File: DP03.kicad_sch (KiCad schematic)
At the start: 21 parts

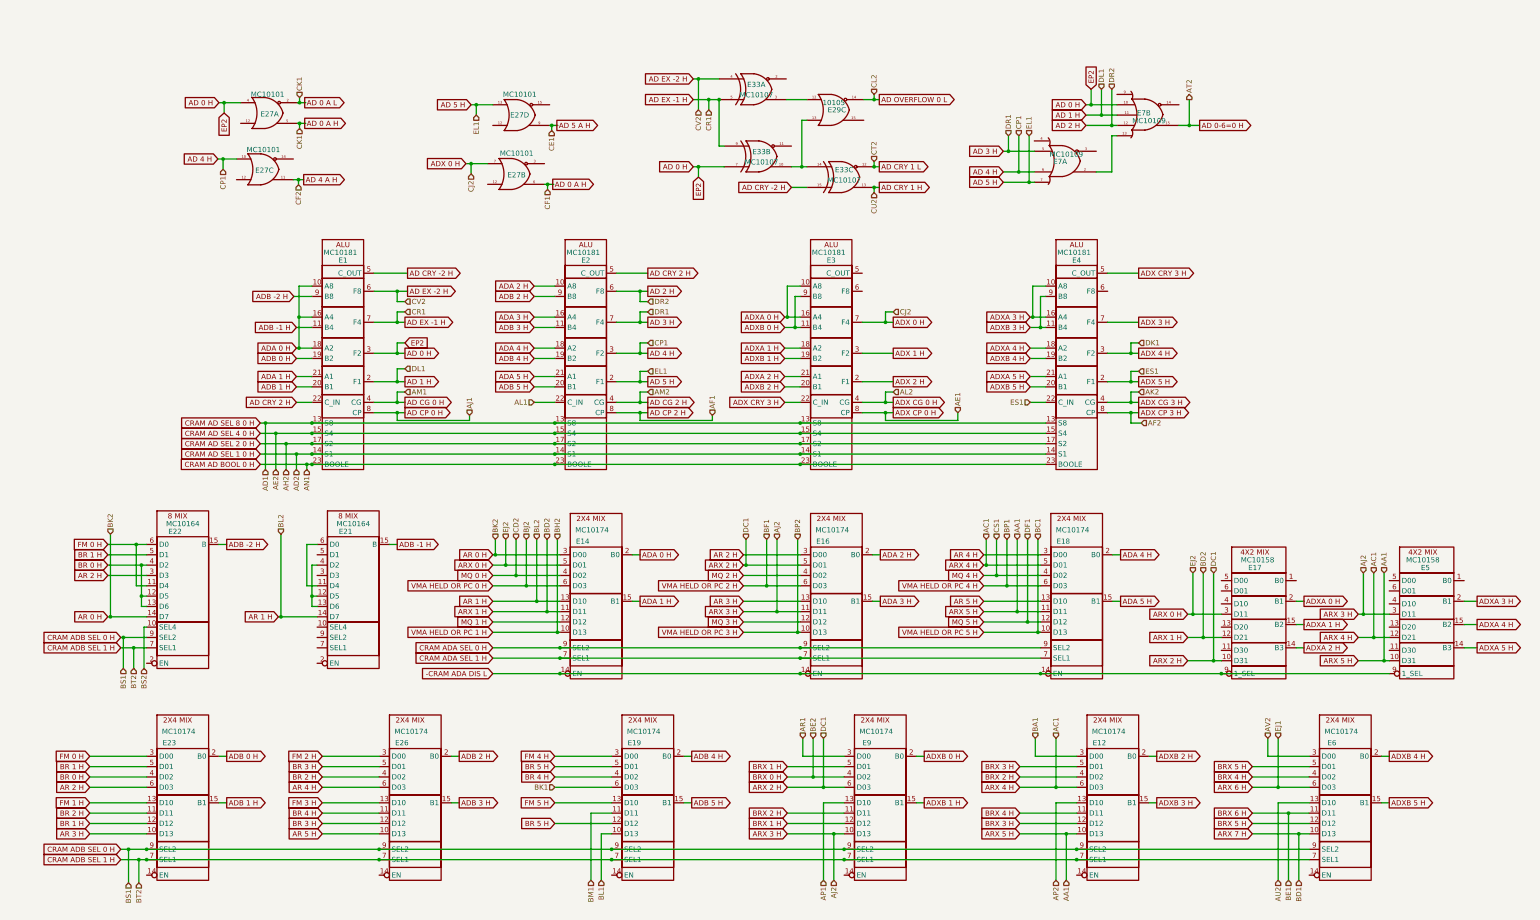
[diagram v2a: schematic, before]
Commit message: Convert all backplane refs to global labels and stick them on J1 pins. Convert all signal labels to global labels too so they are "global" inside M8512 board.
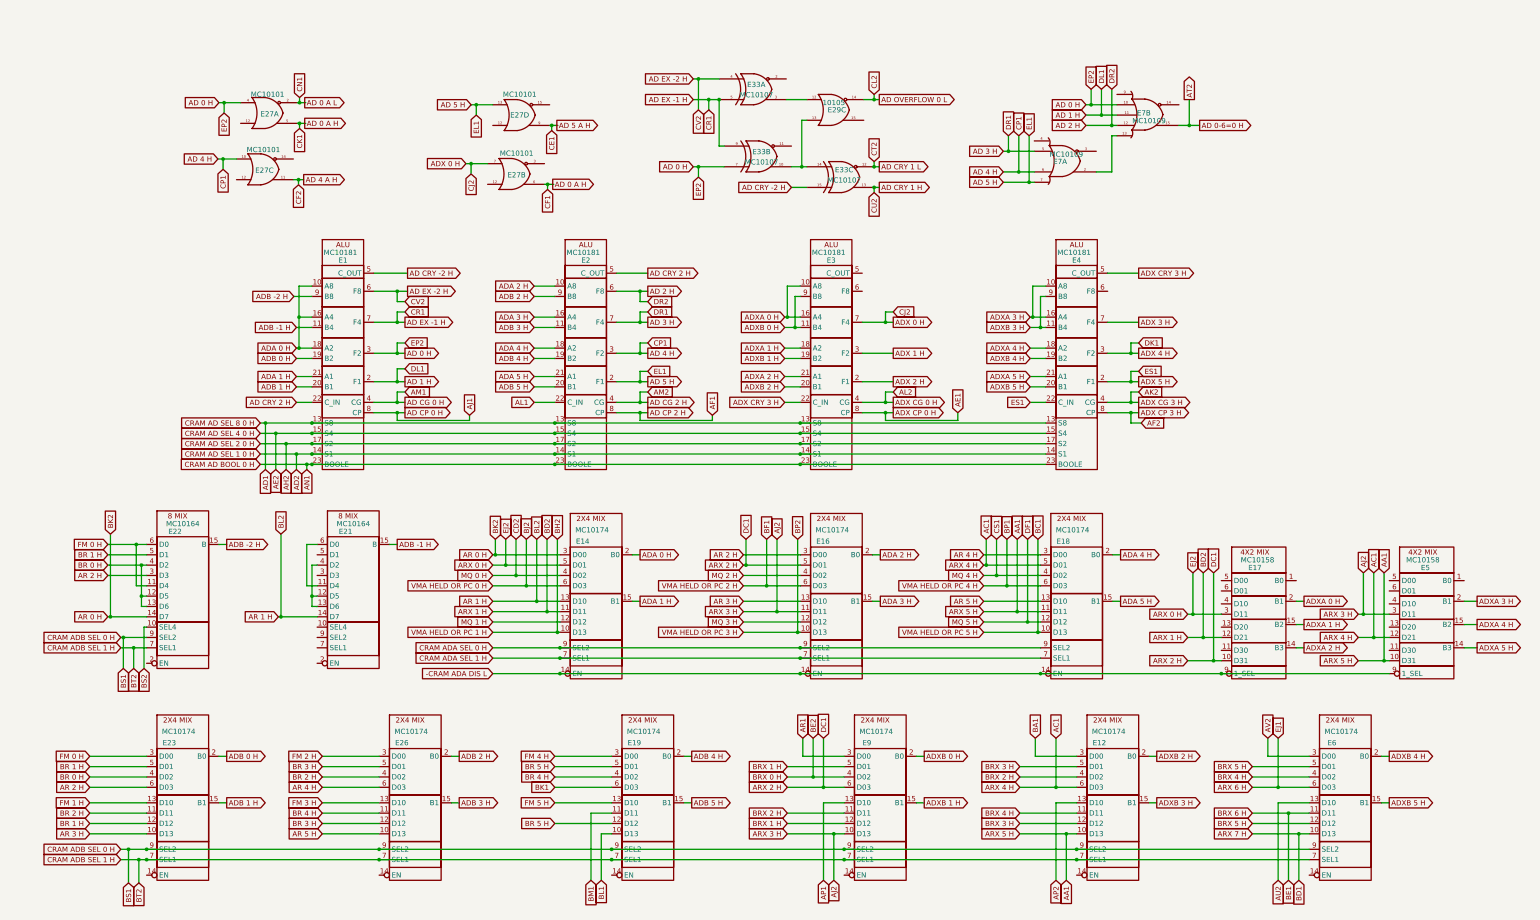
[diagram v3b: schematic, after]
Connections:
- net AD 0 A H: no longer E27.2 (~Aout)
- net ARX 3 H renamed AJ2
- net ARX 4 H renamed AC1
- net ARX 5 H renamed AA1
- net BRX 0 H renamed BE2
- net BRX 6 H renamed BE1
- net CRAM AD BOOL 0 H renamed AN1
- net CRAM AD SEL 1 0 H renamed AD2
- net CRAM AD SEL 2 0 H renamed AH2
- net CRAM AD SEL 4 0 H renamed AE2
- net CRAM AD SEL 8 0 H renamed AD1
- net CRAM ADB SEL 0 H renamed BS1
- net CRAM ADB SEL 1 H renamed BT2
- net MQ 0 H renamed CD2
- net MQ 4 H renamed CS1
- net MQ 5 H renamed DF1
- net VMA HELD OR PC 0 H renamed BJ2
- net VMA HELD OR PC 1 H renamed BH2
- net VMA HELD OR PC 2 H renamed BF1
- net VMA HELD OR PC 3 H renamed BP2
- net VMA HELD OR PC 4 H renamed BP1
- net VMA HELD OR PC 5 H renamed BC1
- new net AD 0 A L: E27.2 (~Aout)

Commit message: checkpoint
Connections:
- net AA1 renamed ARX 5 H <AA1>
- net AC1 renamed ARX 4 H <AC1>
- net AD 0 A H renamed AD 0 A H <CF1>
- net AD 0 A H <CF1>: no longer E27.5 (Aout)
- net AD 0 A L renamed AD 0 A L <CN1>
- net AD 0 H renamed AD 0 H <EP2>
- net AD 0-6=0 H renamed AD 0-6=0 H <AT2>
- net AD 1 H renamed AD 1 H <DL1>
- net AD 2 H renamed AD 2 H <DR2>
- net AD 3 H renamed AD 3 H <DR1>
- net AD 4 A H renamed AD 4 A H <CF2>
- net AD 4 H renamed AD 4 H <CP1>
- net AD 5 A H renamed AD 5 A H <CE1>
- net AD 5 H renamed AD 5 H <EL1>
- net AD CG 0 H renamed AD CG 0 H <AM1>
- net AD CG 2 H renamed AD CG 2 H <AM2>
- net AD CP 0 H renamed AD CP 0 H <AJ1>
- net AD CP 2 H renamed AD CP 2 H <AF1>
- net AD CRY 1 H renamed AD CRY 1 H <CU2>
- net AD CRY 1 L renamed AD CRY 1 L <CT2>
- net AD EX -1 H renamed AD EX -1 H <CR1>
- net AD EX -2 H renamed AD EX -2 H <CV2>
- net AD OVERFLOW 0 L renamed AD OVERFLOW 0 L <CL2>
- net AD1 renamed CRAM AD SEL 8 0 H <AD1>
- net AD2 renamed CRAM AD SEL 1 0 H <AD2>
- net ADX 0 H renamed ADX 0 H <CJ2>
- net ADX 4 H renamed ADX 4 H <DK1>
- net ADX 5 H renamed <ES1>
- net <ES1>: no longer E4.2 (F1)
- net ADX CG 0 H renamed ADX CG 0 H <AL2>
- net ADX CG 3 H renamed ADX CG 3 H <AK2>
- net ADX CP 0 H renamed ADX CP 0 H <AE1>
- net ADX CP 3 H renamed ADX CP 3 H <AF2>
- net AE2 renamed CRAM AD SEL 4 0 H <AE2>
- net AH2 renamed CRAM AD SEL 2 0 H <AH2>
- net AJ2 renamed ARX 3 H <AJ2>
- net AL1 renamed <AL1>
- net AN1 renamed CRAM AD BOOL 0 H <AN1>
- net AP1 renamed <AP1>
- net AP2 renamed <AP2>
- net AR 0 H renamed AR 0 H <BK2>
- net AR 1 H renamed AR 1 H <BL2>
- net AR1 renamed <AR1>
- net ARX 0 H renamed ARX 0 H <EJ2>
- net ARX 1 H renamed ARX 1 H <BD2>
- net ARX 2 H renamed ARX 2 H <DC1>
- net ARX 6 H renamed ARX 6 H <EJ1>
- net ARX 7 H renamed ARX 7 H <BD1>
- net AU2 renamed <AU2>
- net AV2 renamed <AV2>
- net BA1 renamed <BA1>
- net BC1 renamed VMA HELD OR PC 5 H <BC1>
- net BE1 renamed BRX 6 H <BE1>
- net BE2 renamed BRX 0 H <BE2>
- net BF1 renamed VMA HELD OR PC 2 H <BF1>
- net BH2 renamed VMA HELD OR PC 1 H <BH2>
- net BJ2 renamed VMA HELD OR PC 0 H <BJ2>
- net BK1 renamed <BK1>
- net BL1 renamed <BL1>
- net BM1 renamed <BM1>
- net BP1 renamed VMA HELD OR PC 4 H <BP1>
- net BP2 renamed VMA HELD OR PC 3 H <BP2>
- net BS1 renamed CRAM ADB SEL 0 H <BS1>
- net BS2 renamed <BS2>
- net BT2 renamed CRAM ADB SEL 1 H <BT2>
- net CD2 renamed MQ 0 H <CD2>
- net CS1 renamed MQ 4 H <CS1>
- net DF1 renamed MQ 5 H <DF1>
- new net AD 0 A H <CK1>: E27.5 (Aout)
- new net ADX 5 H <ES1>: E4.2 (F1)
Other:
- moved on the sheet: E7A, E7B

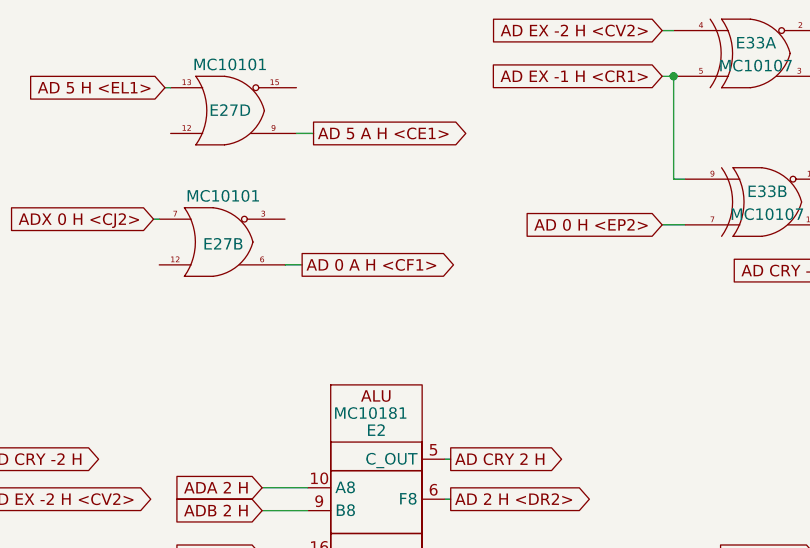
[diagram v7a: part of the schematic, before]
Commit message: Fix a bunch of typos and their backplane signal names
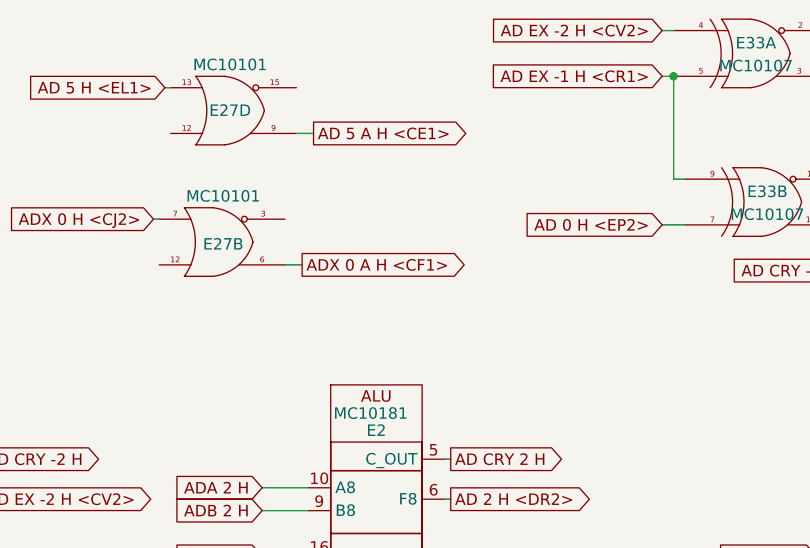
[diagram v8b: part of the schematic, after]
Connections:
- net AD 0 A H <CF1> renamed ADX 0 A H <CF1>
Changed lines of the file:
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@@
     )
   )
-  (global_label "AD 0 A H <CF1>" (shape output) (at 179.705 54.61 0) (fields_autoplaced)
+  (global_label "ADX 0 A H <CF1>" (shape output) (at 179.705 54.61 0) (fields_autoplaced)
     (effects (font (size 1.27 1.27)) (justify left))
-    (property "Intersheet References" "${INTERSHEET_REFS}" (id 0) (at 198.6886 54.5306 0)
+    (property "Intersheet References" "${INTERSHEET_REFS}" (id 0) (at 199.8981 54.5306 0)
       (effects (font (size 1.27 1.27)) (justify left) hide)
     )
